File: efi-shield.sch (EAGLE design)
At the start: 84 parts, among them J1 PWMH, J2 PWMI, J3 COMM, J4 PWR, J5 ADCL, J6 ADCH, J7 AMPSEAL-23POS-HEADER, J8 SPI, Q1 PN2222, Q2 FJPF13009, U1 TXS0104E, U2 TXS0104E, U3 MCP3304, U4 MCP6024, U5 MCP6024, U6 MCP6022, U7 NE555DR, U8 MCP4142-104

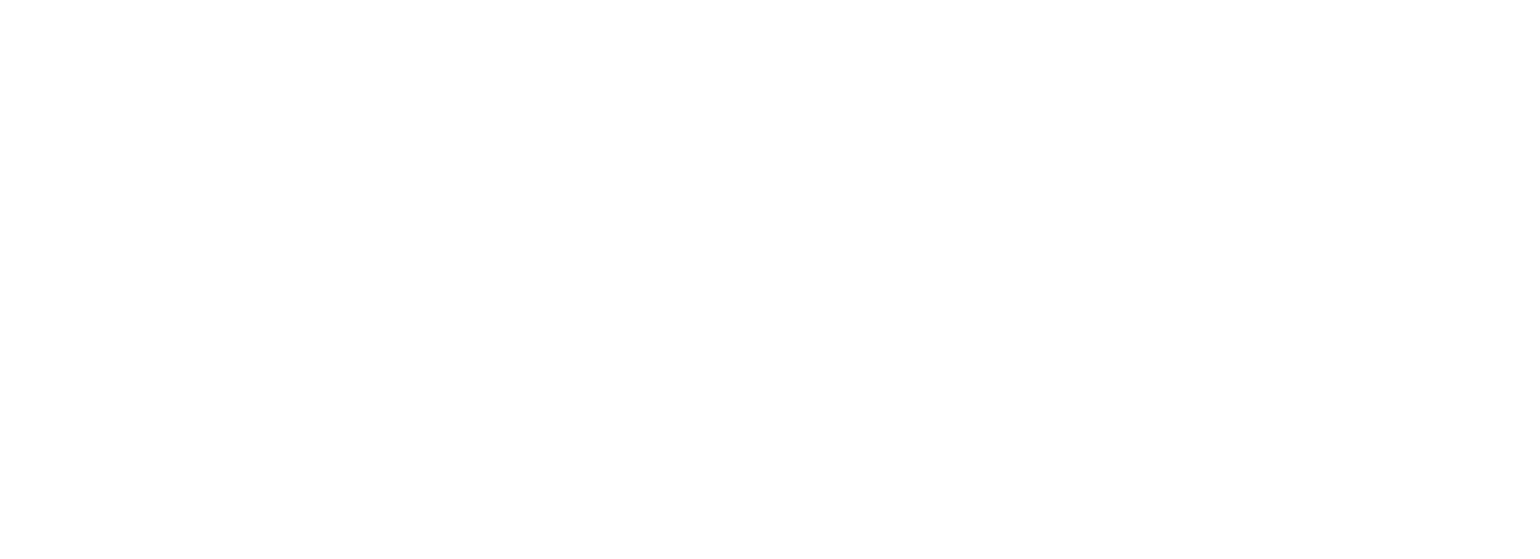
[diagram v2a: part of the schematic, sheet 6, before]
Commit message: Spark + LED circuits complete. Started on CAN. First BOM generation.
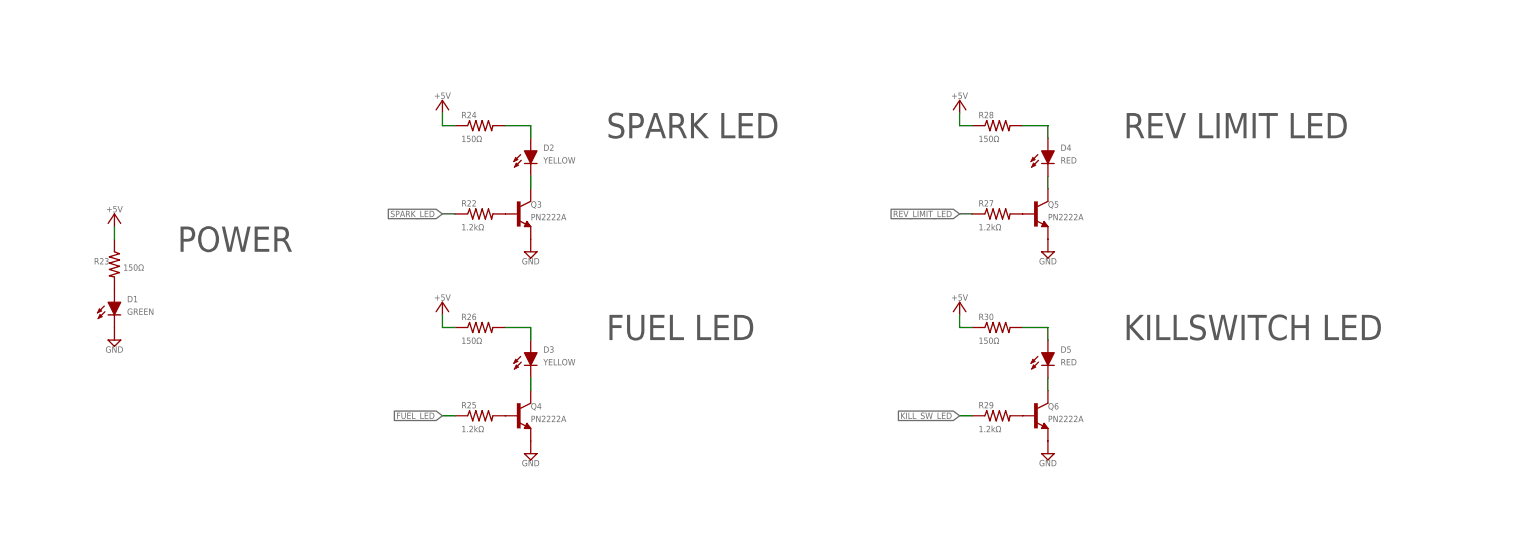
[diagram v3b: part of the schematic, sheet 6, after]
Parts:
- added C33: 0.1uF, cpsmv:CAP-JKE
- added D1: GREEN, cpsmv:LTL-533-11
- added D2, D3: YELLOW, cpsmv:LTL-553-11
- added D4, D5: RED, cpsmv:LTL-523-11
- added Q3, Q4, Q5, Q6: PN2222A, cpsmv:PN2222A
- added Q7: (no value), cpsmv:ISL9V5036P3_F085
- added R22, R25, R27, R29: 1.2kΩ, cpsmv:RES-JKE
- added R23, R24, R26, R28, R30: 150Ω, cpsmv:RES-JKE
- added U10: MCP2551-I/SN, cpsmv:MCP2551-I/SN
- J8: device pinhead:PINHD-2X3 -> cpsmv:PINHD-2X3
- Q1: value PN2222 -> PN2222A; device cpsmv:2N2222 -> cpsmv:PN2222A
- renumbered U$7 to U9
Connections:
- new net CANH: U10.CANH
- new net CANL: U10.CANL
- new net CAN_RX: J6.7, U10.RXD
- new net CAN_TX: J6.8, U10.TXD
- new net FUEL_LED: R25.1
- new net IGN_COIL: Q7.C
- new net KILL_SW_LED: R29.1
- new net N$25: D2.CATHODE, Q3.C
- new net N$26: D2.ANODE, R24.2
- new net N$27: D1.ANODE, R23.2
- new net N$28: Q3.B, R22.2
- new net N$29: D3.CATHODE, Q4.C
- new net N$30: D3.ANODE, R26.2
- new net N$31: Q4.B, R25.2
- new net N$32: D4.CATHODE, Q5.C
- new net N$33: D4.ANODE, R28.2
- new net N$34: Q5.B, R27.2
- new net N$35: D5.CATHODE, Q6.C
- new net N$36: D5.ANODE, R30.2
- new net N$37: Q6.B, R29.2
- new net REV_LIMIT_LED: R27.1
- new net SPARK_LED: R22.1
- net +5V: now also C33.1, R23.1, R24.1, R26.1, R28.1, R30.1
- net GND: now also C33.2, D1.CATHODE, Q3.E, Q4.E, Q5.E, Q6.E, Q7.E, U10.RS, U10.VSS
- net SPARK: now also Q7.G
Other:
- note added: "FUEL LED"
- note added: "KILLSWITCH LED"
- note added: "LAYOUT NOTE: Place decoupling cap as close as possible to the Vdd pin."
- note added: "LAYOUT NOTE: Place within 100mm of 1uf buld capacitor shared with other MCP602x devices."
- note added: "POWER"
- note added: "REV LIMIT LED"
- note added: "SPARK LED"
- note removed: "LAYOUT NOTE: >1uF bulk capacitor is shared with other MCP602x devices on the Analog sheet."
- note removed: "LAYOUT NOTE: Place decoupling cap as close as possible Vdd pin."
- moved on the sheet: Q1, Q2, R1

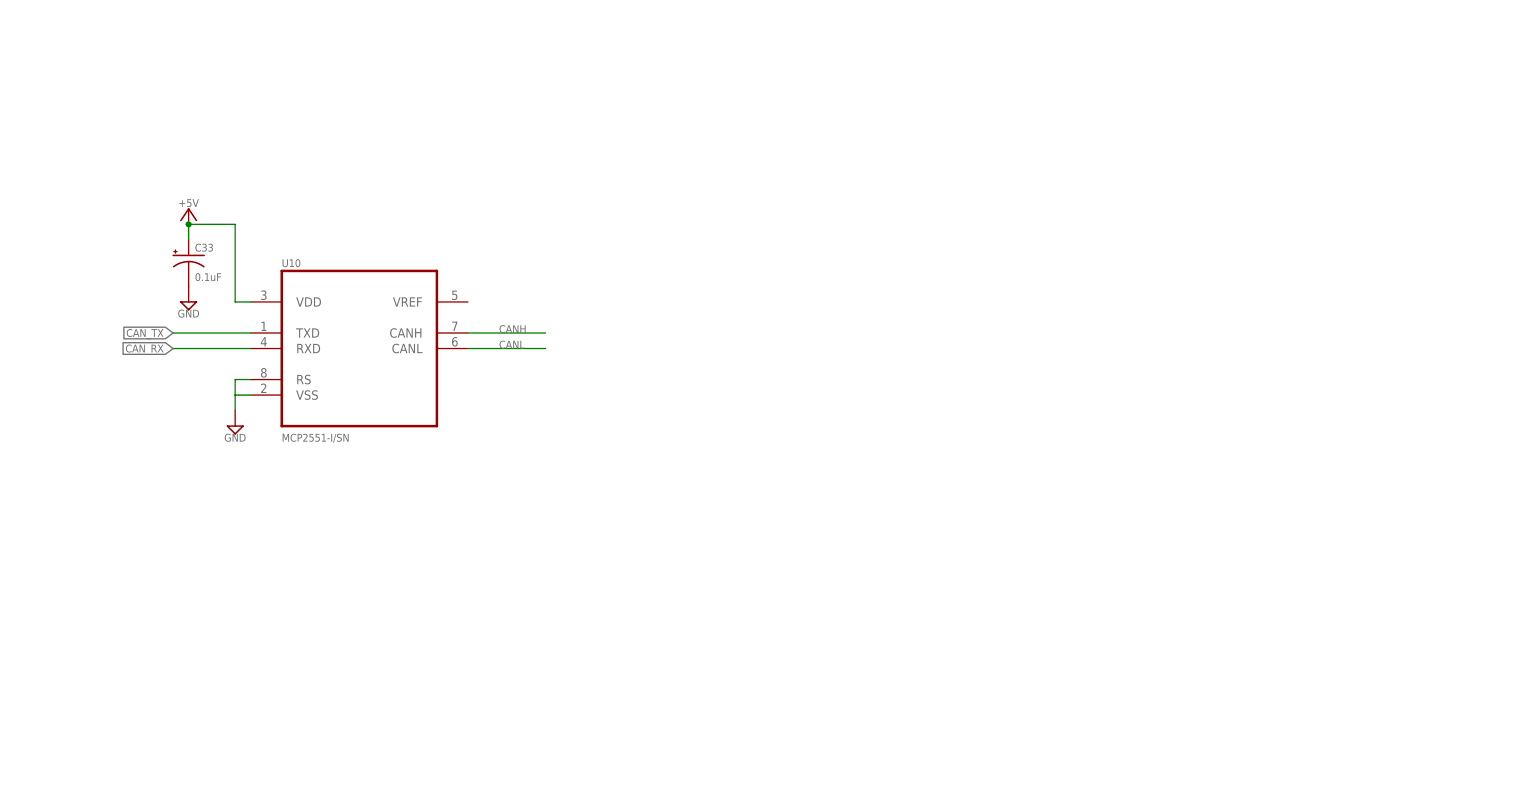
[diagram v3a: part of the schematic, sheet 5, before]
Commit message: CAN complete. Added shunt resistors to spark and fuel circuits.
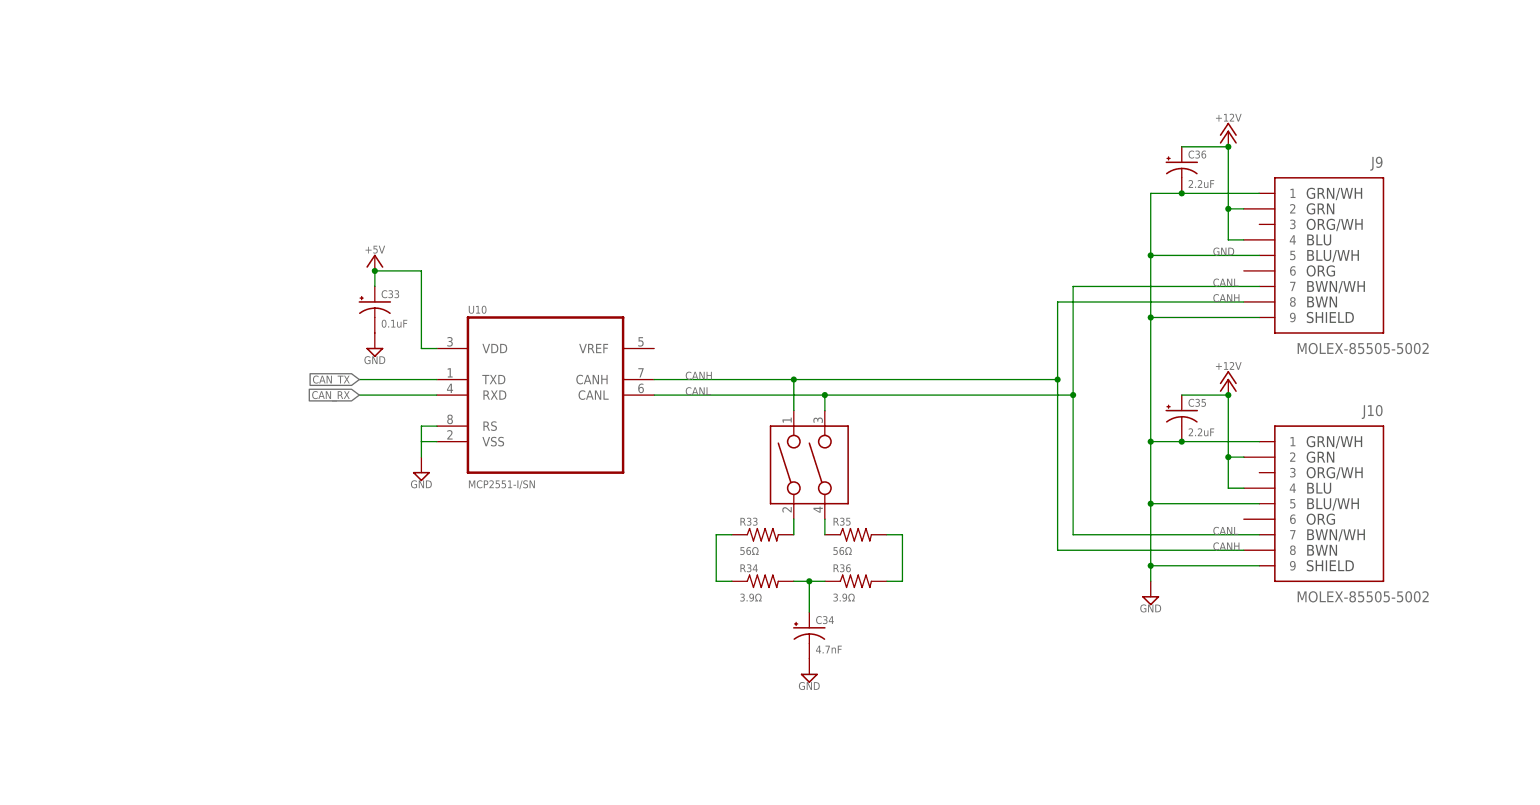
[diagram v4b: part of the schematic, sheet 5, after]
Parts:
- added C34: 4.7nF, cpsmv:CAP-JKE
- added C35, C36: 2.2uF, cpsmv:CAP-JKE
- added J10, J9: MOLEX-85505-5002, cpsmv:MOLEX-85505-5002
- added R31, R32: 10mΩ, cpsmv:VISHAY_DALE-LVR03R0100FE70
- added R33, R35: 56Ω, cpsmv:RES-JKE
- added R34, R36: 3.9Ω, cpsmv:RES-JKE
- added SW1: CTS-204-211ST, cpsmv:CTS-204-211ST
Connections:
- new net N$38: Q7.E, R32.2
- new net N$39: Q2.E, R31.2
- new net N$40: R33.2, SW1.2
- new net N$41: R35.1, SW1.4
- new net N$42: R33.1, R34.1
- new net N$43: R35.2, R36.2
- new net N$44: C34.1, R34.2, R36.1
- net +12V: now also C35.1, C36.1, J10.2, J10.4, J9.2, J9.4
- net +5V: now also U10.VDD
- net CANH: now also J10.8, J9.8, SW1.1
- net CANL: now also J10.7, J9.7, SW1.3
- net GND: now also C34.2, C35.2, C36.2, J10.1, J10.5, J10.9, J9.1, J9.5, J9.9, R31.1, R32.1; no longer Q2.E, Q7.E
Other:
- moved on the sheet: C33, JP1, JP2, JP3, Q1, Q2, R1, U10
